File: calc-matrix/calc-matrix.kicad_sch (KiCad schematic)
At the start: 6 parts, among them J3 LiPo, J4 SD, J5 LCD, SW50 PWR

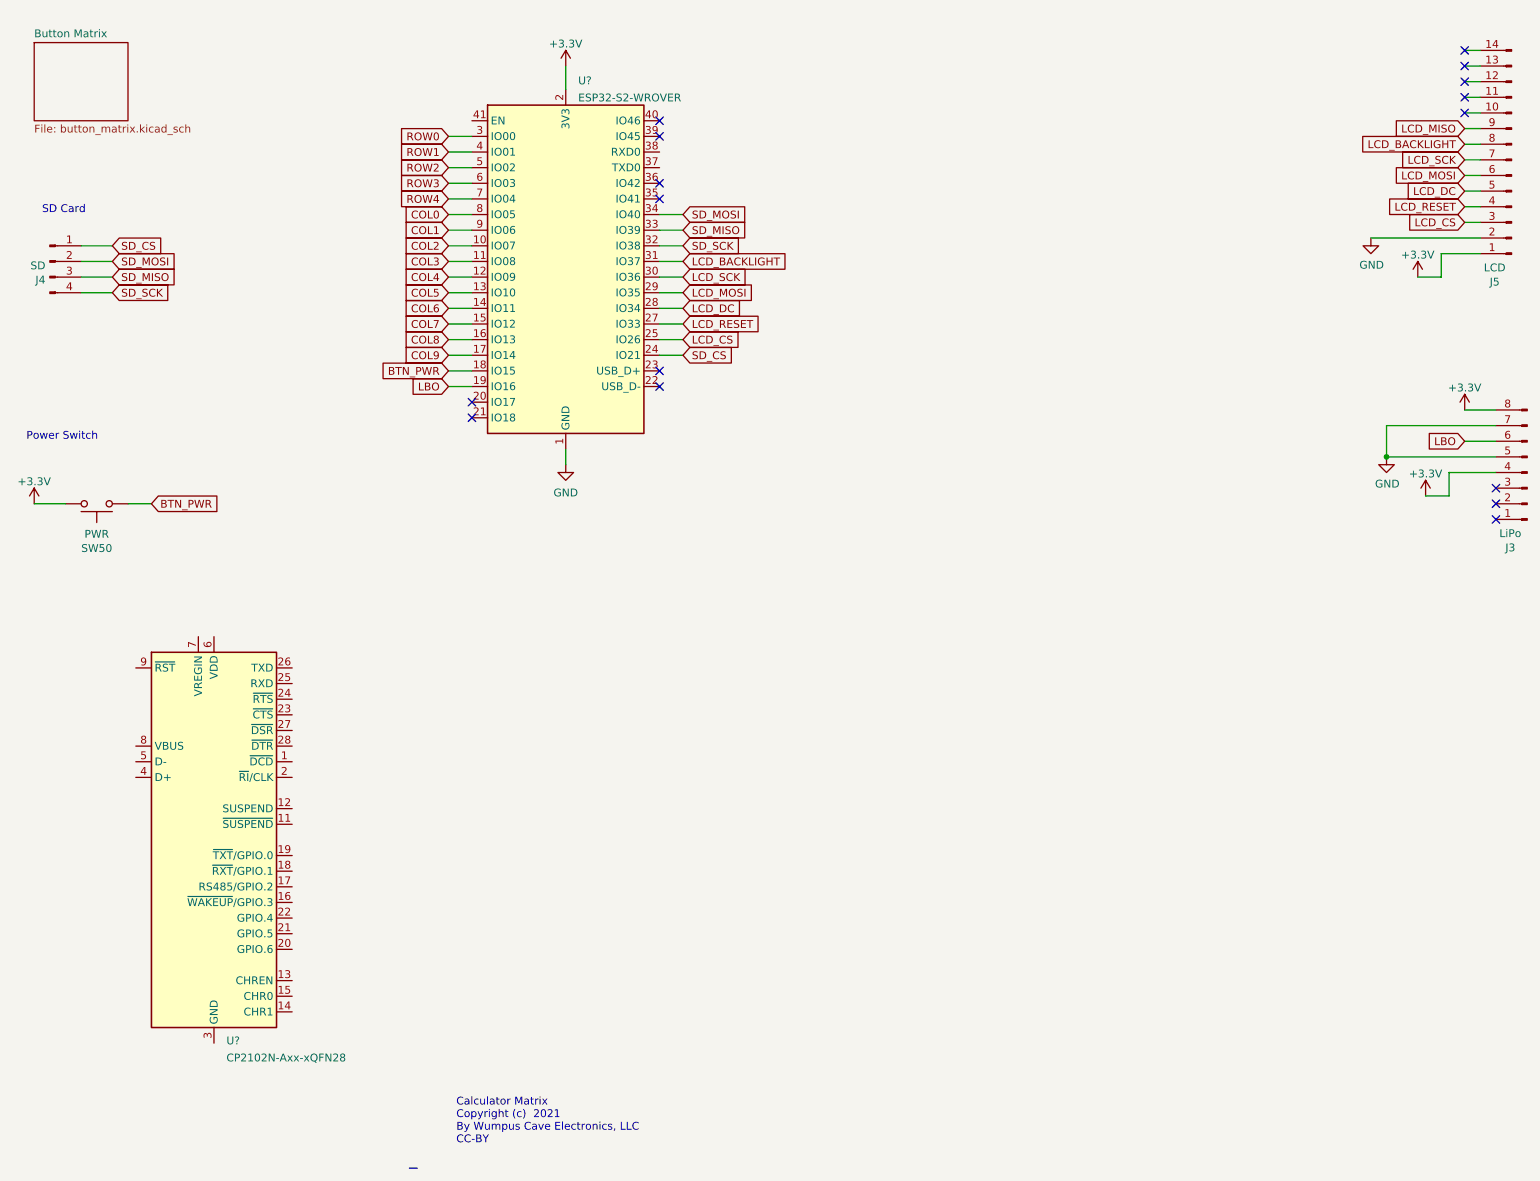
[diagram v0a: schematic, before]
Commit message: Move towards on board power, esp32, and USB
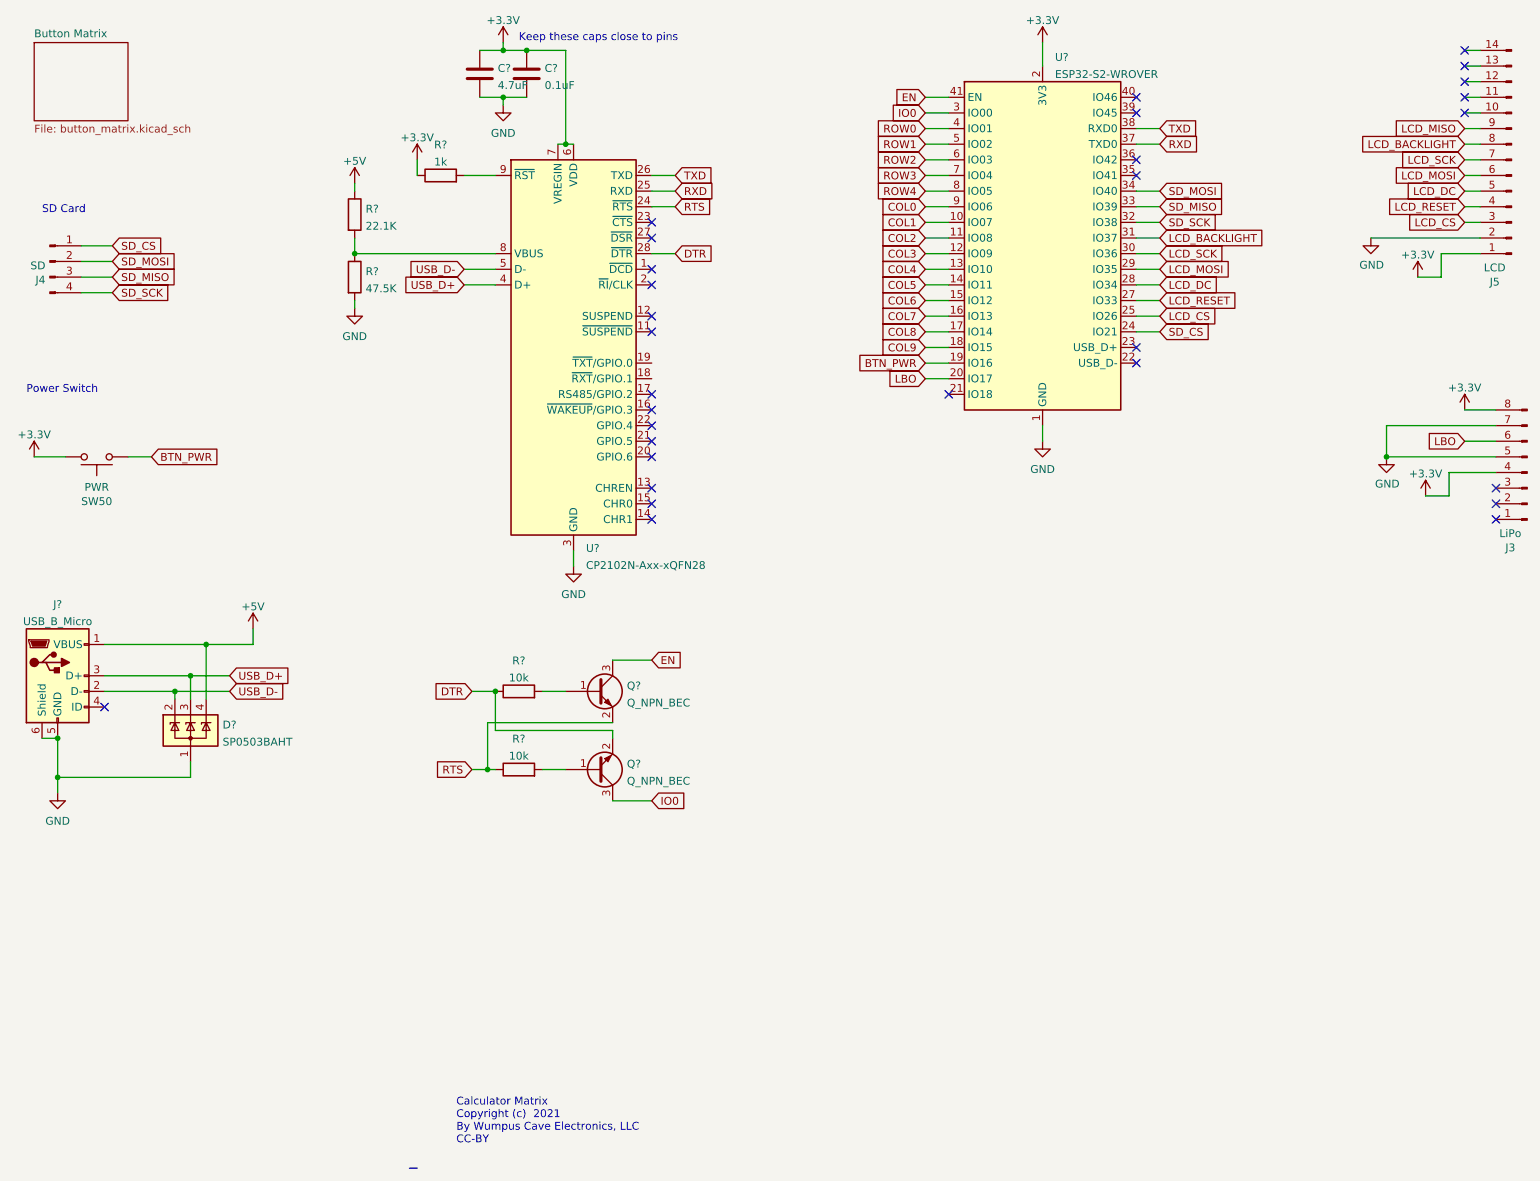
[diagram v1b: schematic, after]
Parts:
- added C?: 0.1uF, Capacitor_SMD:C_0805_2012Metric, symbol Device:C
- added C?: 4.7uF, Capacitor_SMD:C_0805_2012Metric, symbol Device:C
- added D?: SP0503BAHT, Package_TO_SOT_SMD:SOT-143, symbol Power_Protection:SP0503BAHT
- added J?: USB_B_Micro, symbol Connector:USB_B_Micro
- added Q? (x2): Q_NPN_BEC, Package_TO_SOT_SMD:SC-59, symbol Device:Q_NPN_BEC
- added R?: 1k, Resistor_SMD:R_0805_2012Metric, symbol Device:R
- added R? (x2): 10k, Resistor_SMD:R_0805_2012Metric, symbol Device:R
- added R?: 22.1K, Resistor_SMD:R_0805_2012Metric, symbol Device:R
- added R?: 47.5K, Resistor_SMD:R_0805_2012Metric, symbol Device:R
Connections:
- net +3V3: now also U?.6 (VDD), U?.7 (VREGIN), C?.2, C?.2, R?.1
- net BTN_PWR: now also U?.19 (IO16); no longer U?.18 (IO15)
- net COL0: now also U?.9 (IO06); no longer U?.8 (IO05)
- net COL1: now also U?.10 (IO07); no longer U?.9 (IO06)
- net COL2: now also U?.11 (IO08); no longer U?.10 (IO07)
- net COL3: now also U?.12 (IO09); no longer U?.11 (IO08)
- net COL4: now also U?.13 (IO10); no longer U?.12 (IO09)
- net COL5: now also U?.14 (IO11); no longer U?.13 (IO10)
- net COL6: now also U?.15 (IO12); no longer U?.14 (IO11)
- net COL7: now also U?.16 (IO13); no longer U?.15 (IO12)
- net COL8: now also U?.17 (IO14); no longer U?.16 (IO13)
- net COL9: now also U?.18 (IO15); no longer U?.17 (IO14)
- net GND: now also U?.29 (GND), U?.3 (GND), C?.1, C?.1, D?.1 (A), J?.5 (GND), J?.6 (Shield), R?.2
- net LBO: now also U?.20 (IO17); no longer U?.19 (IO16)
- net ROW0: now also U?.4 (IO01); no longer U?.3 (IO00)
- net ROW1: now also U?.5 (IO02); no longer U?.4 (IO01)
- net ROW2: now also U?.6 (IO03); no longer U?.5 (IO02)
- net ROW3: now also U?.7 (IO04); no longer U?.6 (IO03)
- net ROW4: now also U?.8 (IO05); no longer U?.7 (IO04)
- net RXD: now reaches U?.37 (TXD0)
- net RXD: now also U?.25 (RXD)
- net TXD: now reaches U?.38 (RXD0)
- net TXD: now also U?.26 (TXD)
- net EN: now reaches U?.41 (EN)
- net EN: now also Q?.3 (C)
- net RTS: now reaches U?.24 (~{RTS})
- net RTS: now also Q?.2 (E), R?.1
- net DTR: now reaches U?.28 (~{DTR})
- net DTR: now also Q?.2 (E), R?.1
- net USB_D+: now reaches U?.4 (D+)
- net USB_D+: now also D?.3 (K), J?.3 (D+)
- net USB_D-: now reaches U?.5 (D-)
- net USB_D-: now also D?.2 (K), J?.2 (D-)
- net at U?.8 (VBUS): now also R?.1, R?.2
- net at U?.9 (~{RST}): now also R?.2
- new net: Q?.1 (B), R?.2 (x2)
- new net +5V: D?.4 (K), J?.1 (VBUS), R?.1
- new net IO0: Q?.3 (C), U?.3 (IO00)
- no-connect marks 16 -> 30
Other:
- note added: "Keep these caps close to pins"
- moved on the sheet: SW50, U?
